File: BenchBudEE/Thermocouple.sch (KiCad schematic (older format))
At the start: 14 parts

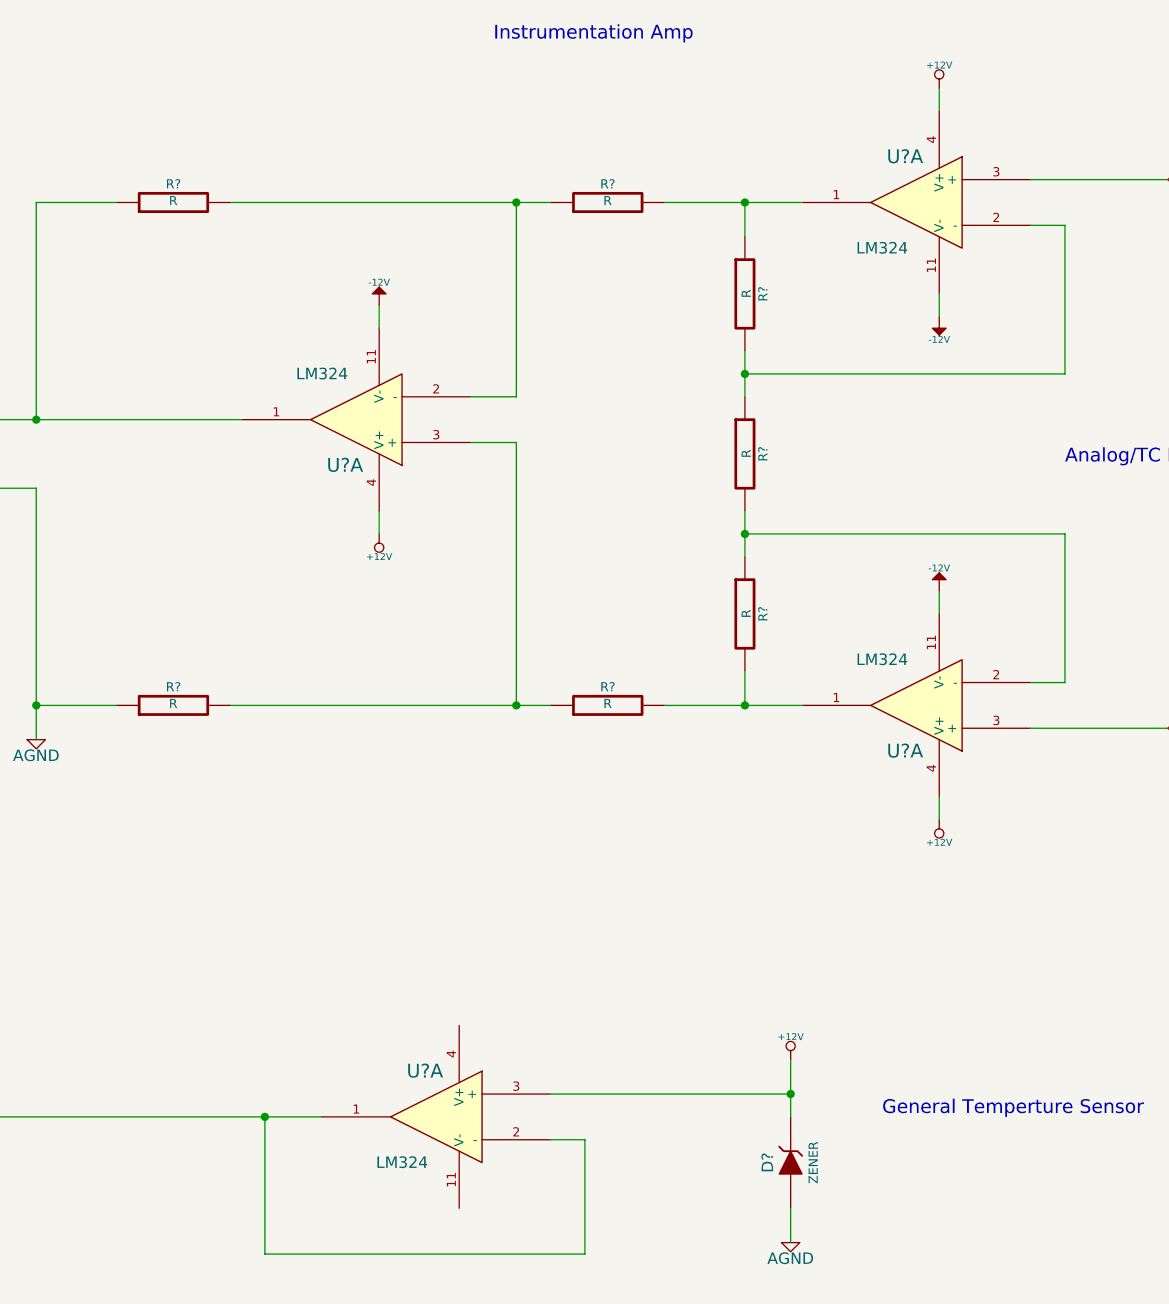
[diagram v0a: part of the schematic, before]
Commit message: Associating and Placing the Relay Module
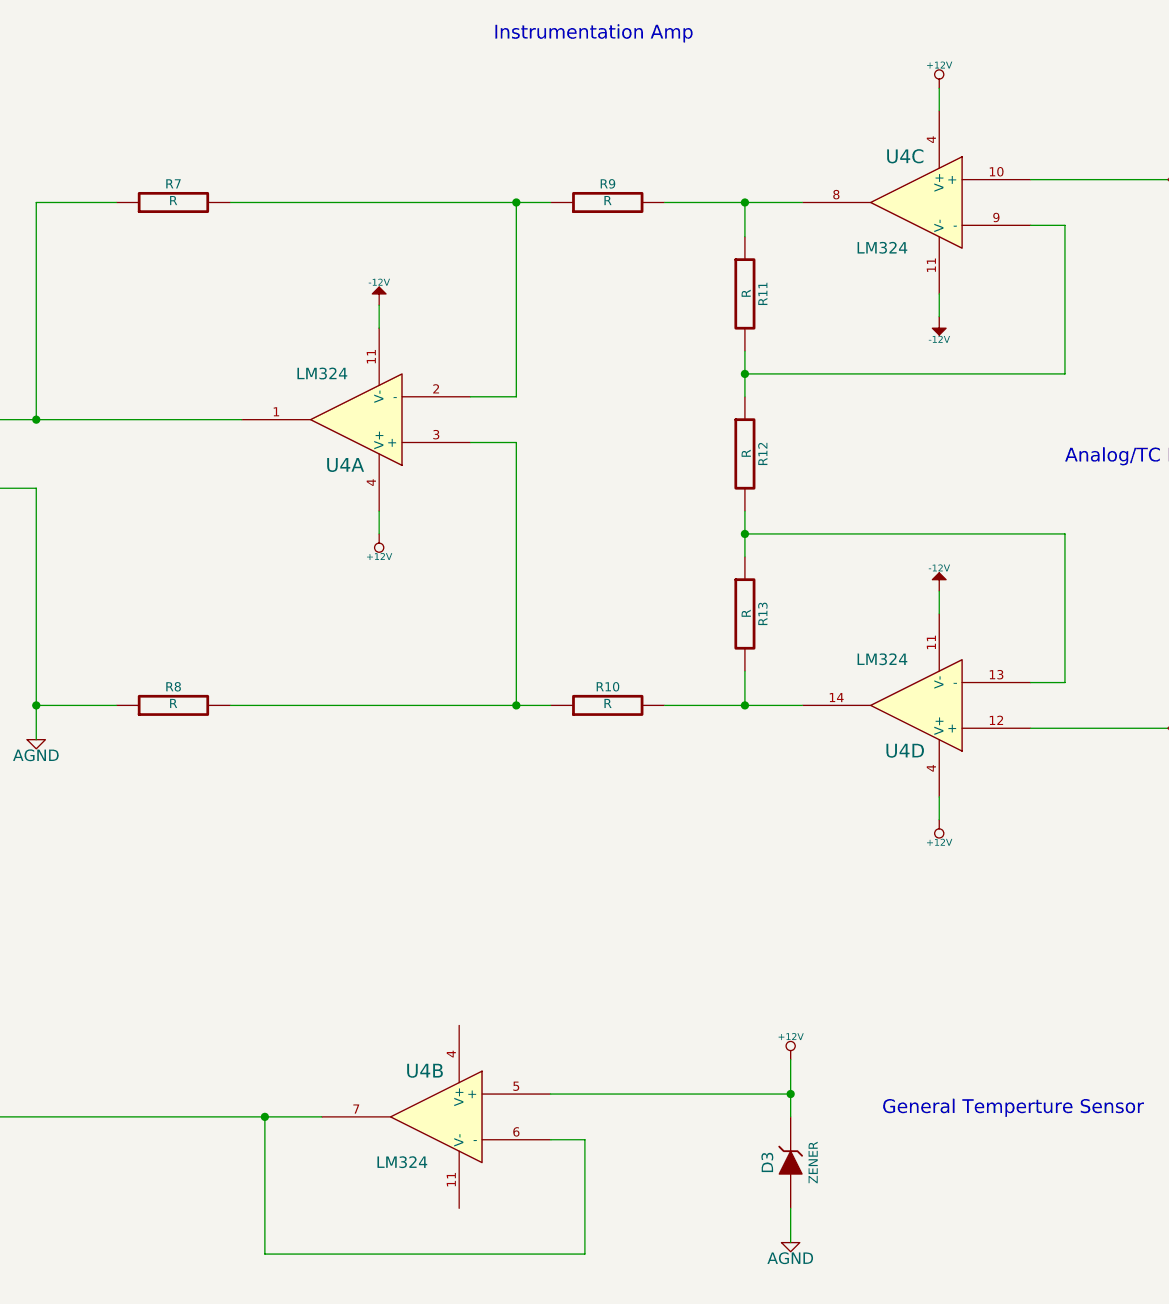
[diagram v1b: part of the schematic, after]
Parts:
- gave numbers to parts that had none: 11
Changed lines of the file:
@@
 CS_N
 $Comp
-L LM324 U?
-U 1 1 52F12A0C
+L LM324 U4
+U 3 1 52F12A0C
 P 9100 2200
-F 0 "U?" H 9150 2400 60  0000 C CNN
+F 0 "U4" H 9150 2400 60  0000 C CNN
 F 1 "LM324" H 9250 2000 50  0000 C CNN
 F 2 "" H 9100 2200 60  0000 C CNN
 F 3 "" H 9100 2200 60  0000 C CNN
-	1    9100 2200
+	3    9100 2200
 	-1   0    0    -1
 $EndComp
 $Comp
-L LM324 U?
-U 1 1 52F12A19
+L LM324 U4
+U 4 1 52F12A19
 P 9100 4400
-F 0 "U?" H 9150 4600 60  0000 C CNN
+F 0 "U4" H 9150 4600 60  0000 C CNN
 F 1 "LM324" H 9250 4200 50  0000 C CNN
 F 2 "" H 9100 4400 60  0000 C CNN
 F 3 "" H 9100 4400 60  0000 C CNN
-	1    9100 4400
-	-1   0    0    1
-$EndComp
-$Comp
-L LM324 U?
+	4    9100 4400
+	-1   0    0    1
+$EndComp
+$Comp
+L LM324 U4
 U 1 1 52F12A1F
 P 6650 3150
-F 0 "U?" H 6700 3350 60  0000 C CNN
+F 0 "U4" H 6700 3350 60  0000 C CNN
 F 1 "LM324" H 6800 2950 50  0000 C CNN
 F 2 "" H 6650 3150 60  0000 C CNN
@@
 $EndComp
 $Comp
-L LM324 U?
-U 1 1 52F12A25
+L LM324 U4
+U 2 1 52F12A25
 P 7000 6200
-F 0 "U?" H 7050 6400 60  0000 C CNN
+F 0 "U4" H 7050 6400 60  0000 C CNN
 F 1 "LM324" H 7150 6000 50  0000 C CNN
 F 2 "" H 7000 6200 60  0000 C CNN
 F 3 "" H 7000 6200 60  0000 C CNN
-	1    7000 6200
+	2    7000 6200
 	-1   0    0    -1
 $EndComp
 $Comp
-L R R?
+L R R11
 U 1 1 52F12AC6
 P 8350 2600
-F 0 "R?" V 8430 2600 40  0000 C CNN
+F 0 "R11" V 8430 2600 40  0000 C CNN
 F 1 "R" V 8357 2601 40  0000 C CNN
 F 2 "~" V 8280 2600 30  0000 C CNN
@@
 $EndComp
 $Comp
-L R R?
+L R R12
 U 1 1 52F12AF6
 P 8350 3300
-F 0 "R?" V 8430 3300 40  0000 C CNN
+F 0 "R12" V 8430 3300 40  0000 C CNN
 F 1 "R" V 8357 3301 40  0000 C CNN
 F 2 "~" V 8280 3300 30  0000 C CNN
@@
 $EndComp
 $Comp
-L R R?
+L R R13
 U 1 1 52F12AFC
 P 8350 4000
-F 0 "R?" V 8430 4000 40  0000 C CNN
+F 0 "R13" V 8430 4000 40  0000 C CNN
 F 1 "R" V 8357 4001 40  0000 C CNN
 F 2 "~" V 8280 4000 30  0000 C CNN
@@
 	8000 4400 8600 4400
 $Comp
-L R R?
+L R R9
 U 1 1 52F12B22
 P 7750 2200
-F 0 "R?" V 7830 2200 40  0000 C CNN
+F 0 "R9" V 7830 2200 40  0000 C CNN
 F 1 "R" V 7757 2201 40  0000 C CNN
 F 2 "~" V 7680 2200 30  0000 C CNN
@@
 $EndComp
 $Comp
-L R R?
+L R R7
 U 1 1 52F12B2E
 P 5850 2200
-F 0 "R?" V 5930 2200 40  0000 C CNN
+F 0 "R7" V 5930 2200 40  0000 C CNN
 F 1 "R" V 5857 2201 40  0000 C CNN
 F 2 "~" V 5780 2200 30  0000 C CNN
@@
 $EndComp
 $Comp
-L R R?
+L R R10
 U 1 1 52F12B34
 P 7750 4400
-F 0 "R?" V 7830 4400 40  0000 C CNN
+F 0 "R10" V 7830 4400 40  0000 C CNN
 F 1 "R" V 7757 4401 40  0000 C CNN
 F 2 "~" V 7680 4400 30  0000 C CNN
@@
 $EndComp
 $Comp
-L R R?
+L R R8
 U 1 1 52F12B3A
 P 5850 4400
-F 0 "R?" V 5930 4400 40  0000 C CNN
+F 0 "R8" V 5930 4400 40  0000 C CNN
 F 1 "R" V 5857 4401 40  0000 C CNN
 F 2 "~" V 5780 4400 30  0000 C CNN
@@
 	10200 2100 9600 2100
 $Comp
-L -12V #PWR01
+L -12V #PWR3
 U 1 1 52F12CF6
 P 6750 2650
-F 0 "#PWR01" H 6750 2780 20  0001 C CNN
+F 0 "#PWR3" H 6750 2780 20  0001 C CNN
 F 1 "-12V" H 6750 2750 30  0000 C CNN
 F 2 "" H 6750 2650 60  0000 C CNN
@@
 $EndComp
 $Comp
-L -12V #PWR02
+L -12V #PWR8
 U 1 1 52F12D03
 P 9200 2700
-F 0 "#PWR02" H 9200 2830 20  0001 C CNN
+F 0 "#PWR8" H 9200 2830 20  0001 C CNN
 F 1 "-12V" H 9200 2800 30  0000 C CNN
 F 2 "" H 9200 2700 60  0000 C CNN
@@
 $EndComp
 $Comp
-L -12V #PWR03
+L -12V #PWR9
 U 1 1 52F12D09
 P 9200 3900
-F 0 "#PWR03" H 9200 4030 20  0001 C CNN
+F 0 "#PWR9" H 9200 4030 20  0001 C CNN
 F 1 "-12V" H 9200 4000 30  0000 C CNN
 F 2 "" H 9200 3900 60  0000 C CNN
@@
 	6750 2650 6750 2750
 $Comp
-L +12V #PWR04
+L +12V #PWR4
 U 1 1 52F12D6E
 P 6750 3650
-F 0 "#PWR04" H 6750 3600 20  0001 C CNN
+F 0 "#PWR4" H 6750 3600 20  0001 C CNN
 F 1 "+12V" H 6750 3750 30  0000 C CNN
 F 2 "" H 6750 3650 60  0000 C CNN
@@
 $EndComp
 $Comp
-L +12V #PWR05
+L +12V #PWR7
 U 1 1 52F12D7B
 P 9200 1700
-F 0 "#PWR05" H 9200 1650 20  0001 C CNN
+F 0 "#PWR7" H 9200 1650 20  0001 C CNN
 F 1 "+12V" H 9200 1800 30  0000 C CNN
 F 2 "" H 9200 1700 60  0000 C CNN
@@
 $EndComp
 $Comp
-L +12V #PWR06
+L +12V #PWR10
 U 1 1 52F12D81
 P 9200 4900
-F 0 "#PWR06" H 9200 4850 20  0001 C CNN
+F 0 "#PWR10" H 9200 4850 20  0001 C CNN
 F 1 "+12V" H 9200 5000 30  0000 C CNN
 F 2 "" H 9200 4900 60  0000 C CNN
@@
 	6750 3550 6750 3650
 $Comp
-L AGND #PWR07
+L AGND #PWR2
 U 1 1 52F12E22
 P 5250 4550
-F 0 "#PWR07" H 5250 4550 40  0001 C CNN
+F 0 "#PWR2" H 5250 4550 40  0001 C CNN
 F 1 "AGND" H 5250 4480 50  0000 C CNN
 F 2 "" H 5250 4550 60  0000 C CNN
@@
 	5250 3450 5250 4550
 $Comp
-L MCP3550-60-E/SN U?
+L MCP3550-60-E/SN U3
 U 1 1 52F12E64
 P 2400 3300
-F 0 "U?" H 1850 3650 40  0000 C CNN
+F 0 "U3" H 1850 3650 40  0000 C CNN
 F 1 "MCP3550-60-E/SN" H 2100 3600 40  0000 C CNN
 F 2 "SO8" H 2200 3300 30  0000 C CIN
@@
 	1050 3400 1900 3400
 $Comp
-L MCP3550-60-E/SN U?
+L MCP3550-60-E/SN U2
 U 1 1 52F12FCA
 P 2350 6350
-F 0 "U?" H 1800 6700 40  0000 C CNN
+F 0 "U2" H 1800 6700 40  0000 C CNN
 F 1 "MCP3550-60-E/SN" H 2050 6650 40  0000 C CNN
 F 2 "SO8" H 2150 6350 30  0000 C CIN
@@
 $EndComp
 $Comp
-L ZENER D?
+L ZENER D3
 U 1 1 52F13038
 P 8550 6400
-F 0 "D?" H 8550 6500 50  0000 C CNN
+F 0 "D3" H 8550 6500 50  0000 C CNN
 F 1 "ZENER" H 8550 6300 40  0000 C CNN
 F 2 "~" H 8550 6400 60  0000 C CNN
@@
 $EndComp
 $Comp
-L +12V #PWR08
+L +12V #PWR5
 U 1 1 52F13045
 P 8550 5950
-F 0 "#PWR08" H 8550 5900 20  0001 C CNN
+F 0 "#PWR5" H 8550 5900 20  0001 C CNN
 F 1 "+12V" H 8550 6050 30  0000 C CNN
 F 2 "" H 8550 5950 60  0000 C CNN
@@
 $EndComp
 $Comp
-L AGND #PWR09
+L AGND #PWR6
 U 1 1 52F1304C
 P 8550 6750
-F 0 "#PWR09" H 8550 6750 40  0001 C CNN
+F 0 "#PWR6" H 8550 6750 40  0001 C CNN
 F 1 "AGND" H 8550 6680 50  0000 C CNN
 F 2 "" H 8550 6750 60  0000 C CNN
@@
 	3000 6500 3000 6800
 $Comp
-L AGND #PWR010
+L AGND #PWR1
 U 1 1 52F13178
 P 3000 6800
-F 0 "#PWR010" H 3000 6800 40  0001 C CNN
+F 0 "#PWR1" H 3000 6800 40  0001 C CNN
 F 1 "AGND" H 3000 6730 50  0000 C CNN
 F 2 "" H 3000 6800 60  0000 C CNN

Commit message: Associating and Placingthe Thermocouple Module
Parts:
- removed U2, U3: MCP3550-60-E/SN, SO8, symbol MCP3550-60-E/SN
- removed unit 2 of U4
- added C10, C11, C6, C7, C8, C9: C, ~, symbol C
- added P2: CONN_3X2, symbol CONN_3X2
- added P3: CONN_2, symbol CONN_2
- added R44, R45: R, ~, symbol R
- added R48, R49: 0, ~, symbol R
- added U2: MCP3901, symbol MCP3901
- added U3: LMT84, symbol LMT84
- U4: value LM324 -> OPA4170
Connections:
- net labels added: +5V, CH0+, CH0-, CH1+, CH1-, REF+, REF-, ~CS, ~DR, ~RESET
- net labels removed: CS_N
- wire segments 45 -> 103
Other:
- note added: "TEMP SENSOR"
- moved on the sheet: R12

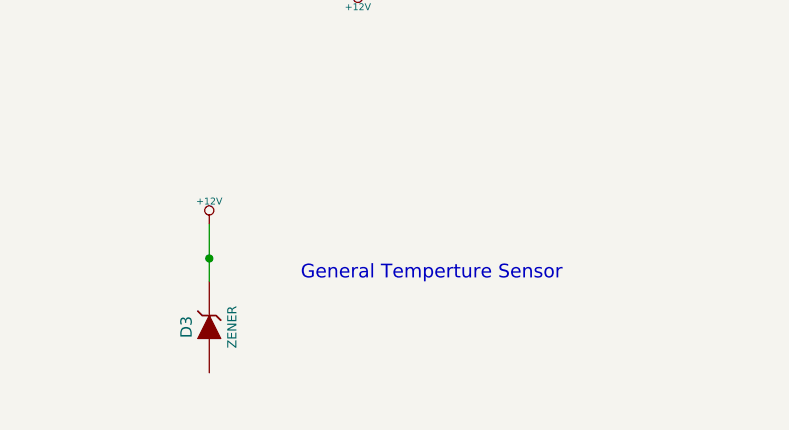
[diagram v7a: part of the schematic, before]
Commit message: Finalizing the system part placement
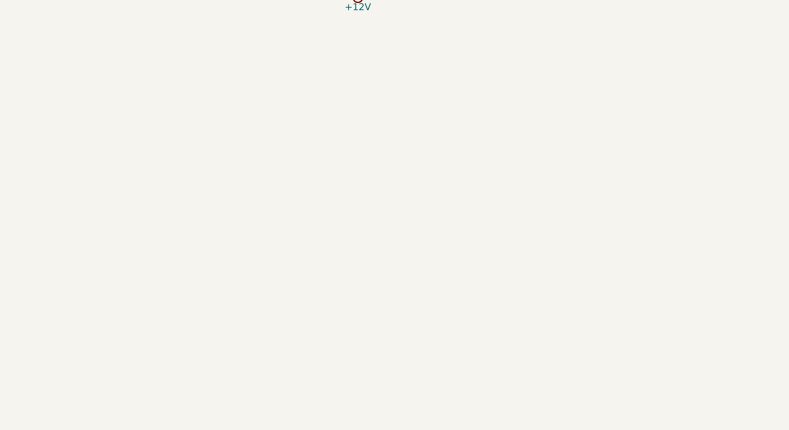
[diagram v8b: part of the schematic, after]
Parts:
- removed D3: ZENER, ~, symbol ZENER
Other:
- note removed: "General Temperture Sensor"
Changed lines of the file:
@@
 $EndComp
 $Comp
-L -12V #PWR12
+L -12V #PWR01
 U 1 1 52F12CF6
 P 6750 2600
-F 0 "#PWR12" H 6750 2730 20  0001 C CNN
+F 0 "#PWR01" H 6750 2730 20  0001 C CNN
 F 1 "-12V" H 6750 2700 30  0000 C CNN
 F 2 "" H 6750 2600 60  0000 C CNN
@@
 $EndComp
 $Comp
-L -12V #PWR16
+L -12V #PWR02
 U 1 1 52F12D03
 P 9200 2700
-F 0 "#PWR16" H 9200 2830 20  0001 C CNN
+F 0 "#PWR02" H 9200 2830 20  0001 C CNN
 F 1 "-12V" H 9200 2800 30  0000 C CNN
 F 2 "" H 9200 2700 60  0000 C CNN
@@
 $EndComp
 $Comp
-L -12V #PWR17
+L -12V #PWR03
 U 1 1 52F12D09
 P 9200 3900
-F 0 "#PWR17" H 9200 4030 20  0001 C CNN
+F 0 "#PWR03" H 9200 4030 20  0001 C CNN
 F 1 "-12V" H 9200 4000 30  0000 C CNN
 F 2 "" H 9200 3900 60  0000 C CNN
@@
 $EndComp
 $Comp
-L +12V #PWR13
+L +12V #PWR04
 U 1 1 52F12D6E
 P 6750 3650
-F 0 "#PWR13" H 6750 3600 20  0001 C CNN
+F 0 "#PWR04" H 6750 3600 20  0001 C CNN
 F 1 "+12V" H 6750 3750 30  0000 C CNN
 F 2 "" H 6750 3650 60  0000 C CNN
@@
 $EndComp
 $Comp
-L +12V #PWR15
+L +12V #PWR05
 U 1 1 52F12D7B
 P 9200 1700
-F 0 "#PWR15" H 9200 1650 20  0001 C CNN
+F 0 "#PWR05" H 9200 1650 20  0001 C CNN
 F 1 "+12V" H 9200 1800 30  0000 C CNN
 F 2 "" H 9200 1700 60  0000 C CNN
@@
 $EndComp
 $Comp
-L +12V #PWR18
+L +12V #PWR06
 U 1 1 52F12D81
 P 9200 4900
-F 0 "#PWR18" H 9200 4850 20  0001 C CNN
+F 0 "#PWR06" H 9200 4850 20  0001 C CNN
 F 1 "+12V" H 9200 5000 30  0000 C CNN
 F 2 "" H 9200 4900 60  0000 C CNN
@@
 $EndComp
 $Comp
-L AGND #PWR7
+L AGND #PWR07
 U 1 1 52F12E22
 P 5250 4550
-F 0 "#PWR7" H 5250 4550 40  0001 C CNN
+F 0 "#PWR07" H 5250 4550 40  0001 C CNN
 F 1 "AGND" H 5250 4480 50  0000 C CNN
 F 2 "" H 5250 4550 60  0000 C CNN
@@
 $EndComp
 $Comp
-L ZENER D3
-U 1 1 52F13038
-P 8550 6400
-F 0 "D3" H 8550 6500 50  0000 C CNN
-F 1 "ZENER" H 8550 6300 40  0000 C CNN
-F 2 "~" H 8550 6400 60  0000 C CNN
-F 3 "~" H 8550 6400 60  0000 C CNN
-	1    8550 6400
-	0    -1   -1   0
-$EndComp
-$Comp
-L +12V #PWR14
-U 1 1 52F13045
-P 8550 5950
-F 0 "#PWR14" H 8550 5900 20  0001 C CNN
-F 1 "+12V" H 8550 6050 30  0000 C CNN
-F 2 "" H 8550 5950 60  0000 C CNN
-F 3 "" H 8550 5950 60  0000 C CNN
-	1    8550 5950
-	1    0    0    -1
-$EndComp
-$Comp
-L AGND #PWR8
+L AGND #PWR08
 U 1 1 52F1304C
 P 5250 6650
-F 0 "#PWR8" H 5250 6650 40  0001 C CNN
+F 0 "#PWR08" H 5250 6650 40  0001 C CNN
 F 1 "AGND" H 5250 6580 50  0000 C CNN
 F 2 "" H 5250 6650 60  0000 C CNN
@@
 	1    0    0    -1
 $EndComp
-Text Notes 8950 6200 0    60   ~ 0
-General Temperture Sensor
 Text Notes 10100 2500 0    60   ~ 0
 Analog/TC Input
@@
 $EndComp
 $Comp
-L +5V #PWR9
+L +5V #PWR09
 U 1 1 5303ACCB
 P 5800 4800
-F 0 "#PWR9" H 5800 4890 20  0001 C CNN
+F 0 "#PWR09" H 5800 4890 20  0001 C CNN
 F 1 "+5V" H 5800 4890 30  0000 C CNN
 F 2 "" H 5800 4800 60  0000 C CNN
@@
 $EndComp
 $Comp
-L AGND #PWR11
+L AGND #PWR010
 U 1 1 5303AEFA
 P 6050 3700
-F 0 "#PWR11" H 6050 3700 40  0001 C CNN
+F 0 "#PWR010" H 6050 3700 40  0001 C CNN
 F 1 "AGND" H 6050 3630 50  0000 C CNN
 F 2 "" H 6050 3700 60  0000 C CNN
@@
 $EndComp
 $Comp
-L AGND #PWR10
+L AGND #PWR011
 U 1 1 5303AFBF
 P 6050 2750
-F 0 "#PWR10" H 6050 2750 40  0001 C CNN
+F 0 "#PWR011" H 6050 2750 40  0001 C CNN
 F 1 "AGND" H 6050 2680 50  0000 C CNN
 F 2 "" H 6050 2750 60  0000 C CNN
@@
 $EndComp
 $Comp
-L +5V #PWR4
+L +5V #PWR012
 U 1 1 5303B53D
 P 3200 1550
-F 0 "#PWR4" H 3200 1640 20  0001 C CNN
+F 0 "#PWR012" H 3200 1640 20  0001 C CNN
 F 1 "+5V" H 3200 1640 30  0000 C CNN
 F 2 "" H 3200 1550 60  0000 C CNN
@@
 $EndComp
 $Comp
-L AGND #PWR6
+L AGND #PWR013
 U 1 1 5303B6E8
 P 3850 1800
-F 0 "#PWR6" H 3850 1800 40  0001 C CNN
+F 0 "#PWR013" H 3850 1800 40  0001 C CNN
 F 1 "AGND" H 3850 1730 50  0000 C CNN
 F 2 "" H 3850 1800 60  0000 C CNN
@@
 $EndComp
 $Comp
-L AGND #PWR3
+L AGND #PWR014
 U 1 1 5303B92C
 P 2650 4550
-F 0 "#PWR3" H 2650 4550 40  0001 C CNN
+F 0 "#PWR014" H 2650 4550 40  0001 C CNN
 F 1 "AGND" H 2650 4480 50  0000 C CNN
 F 2 "" H 2650 4550 60  0000 C CNN
@@
 $EndComp
 $Comp
-L AGND #PWR5
+L AGND #PWR015
 U 1 1 5303BA18
 P 3200 4550
-F 0 "#PWR5" H 3200 4550 40  0001 C CNN
+F 0 "#PWR015" H 3200 4550 40  0001 C CNN
 F 1 "AGND" H 3200 4480 50  0000 C CNN
 F 2 "" H 3200 4550 60  0000 C CNN
@@
 $EndComp
 $Comp
-L +5V #PWR2
+L +5V #PWR016
 U 1 1 5303BA92
 P 2650 1550
-F 0 "#PWR2" H 2650 1640 20  0001 C CNN
+F 0 "#PWR016" H 2650 1640 20  0001 C CNN
 F 1 "+5V" H 2650 1640 30  0000 C CNN
 F 2 "" H 2650 1550 60  0000 C CNN
@@
 $EndComp
 $Comp
-L AGND #PWR1
+L AGND #PWR017
 U 1 1 5303BA98
 P 1950 1800
-F 0 "#PWR1" H 1950 1800 40  0001 C CNN
+F 0 "#PWR017" H 1950 1800 40  0001 C CNN
 F 1 "AGND" H 1950 1730 50  0000 C CNN
 F 2 "" H 1950 1800 60  0000 C CNN
@@
 Connection ~ 5250 4400
 Wire Wire Line
-	8550 5950 8550 6200
-Wire Wire Line
 	5250 6500 5250 6650
-Connection ~ 8550 6100
 Wire Wire Line
 	4250 3250 5250 3250
